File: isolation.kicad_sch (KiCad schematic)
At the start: 39 parts, among them J2 NAPPE_FILAMENT_HT, U1 UCC27517, U12 UCC24612, U13 SN74LVC1G08, U3 ISO7710, U5 DPC817, U7 AMC0311R, U8 AMC0311R, U9 AMC0302R

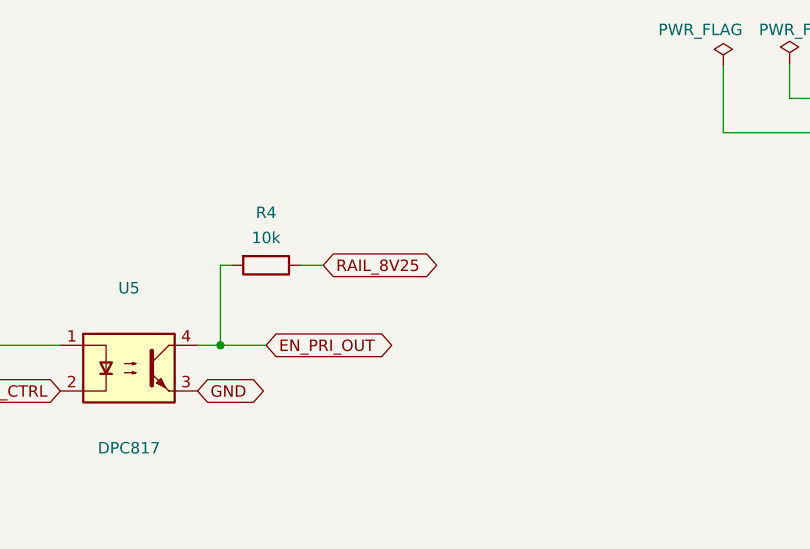
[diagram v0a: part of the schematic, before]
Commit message: Retouches manuelles : notation ~{} pour nPRE/nQ_TRIP, RAIL_8V25->RAIL_3V3_PRI, via 1.0/0.4mm
Renomme nPRE et nQ_TRIP en notation KiCad overline (~{PRE}/~{Q_TRIP}),
corrige une etiquette RAIL_8V25 en RAIL_3V3_PRI dans isolation.kicad_sch,
ajuste la taille de via par defaut (1.8/0.8 -> 1.0/0.4mm) et progresse sur
le placement/routage PCB.

Co-Authored-By: Claude Sonnet 5 <noreply@anthropic.com>
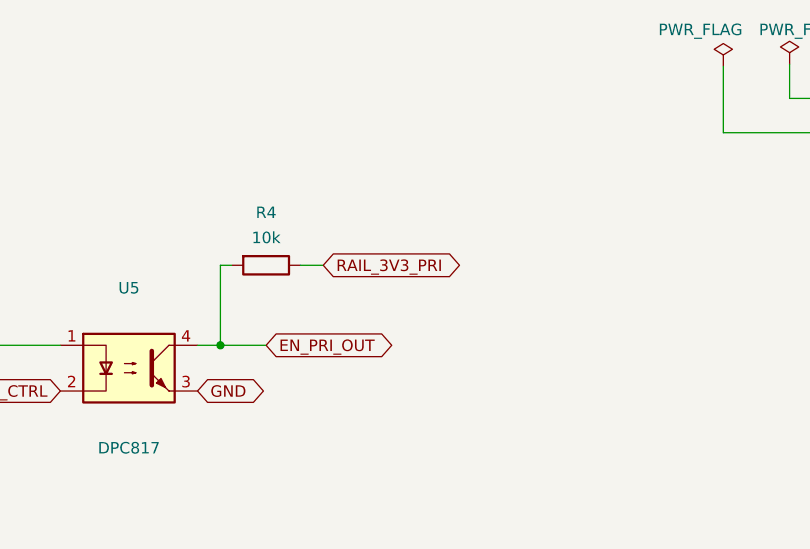
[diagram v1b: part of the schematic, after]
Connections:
- net RAIL_3V3_PRI: now also R4.1
- net RAIL_8V25: no longer R4.1
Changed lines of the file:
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@@
+		)
+	)
+	(global_label "RAIL_3V3_PRI"
+		(shape bidirectional)
+		(at 141.478 50.292 0)
+		(fields_autoplaced yes)
+		(effects
+			(font
+				(size 1.27 1.27)
+			)
+			(justify left)
+		)
+		(property "Intersheetrefs" "${INTERSHEET_REFS}"
+			(at 158.1536 50.292 0)
+			(hide yes)
+			(show_name no)
+			(do_not_autoplace no)
+			(effects
+				(font
+					(size 1.27 1.27)
+				)
+				(justify left)
+			)
 		)
 	)
@@
 			)
 		)
-	)
-	(global_label "RAIL_8V25"
-		(shape bidirectional)
-		(at 141.478 50.292 0)
-		(fields_autoplaced yes)
-		(effects
-			(font
-				(size 1.27 1.27)
-			)
-			(justify left)
-		)
-		(property "Intersheetrefs" "${INTERSHEET_REFS}"
-			(at 155.2507 50.292 0)
-			(hide yes)
-			(show_name no)
-			(do_not_autoplace no)
-			(effects
-				(font
-					(size 1.27 1.27)
-				)
-				(justify left)
-			)
-		)

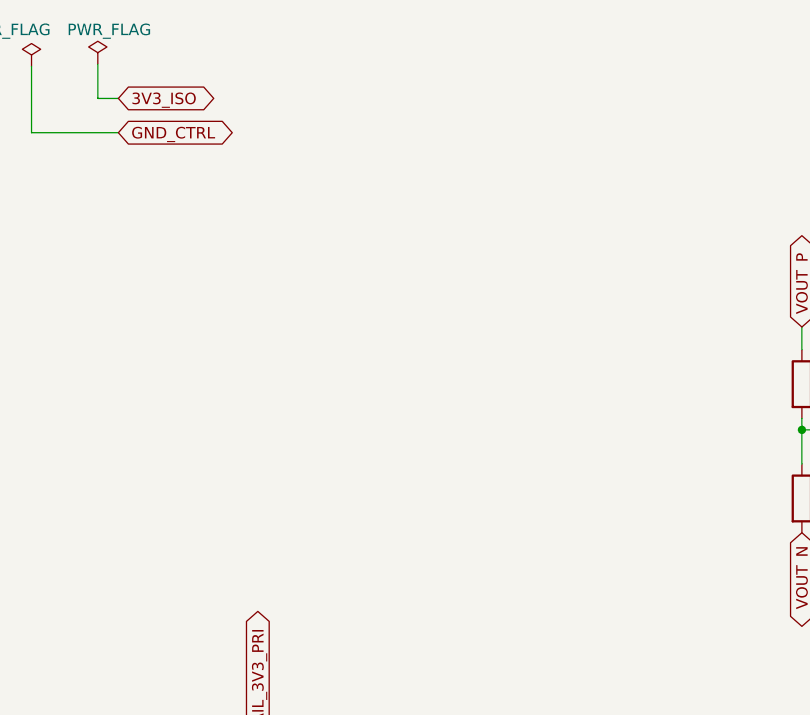
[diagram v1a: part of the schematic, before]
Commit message: Resistances de reference inter-domaines (3x1M par barriere), F1 a 3A
Ajoute les trois chaines de resistances 1M en serie (R35/R6/R36,
R37/R38/R39, R42/R41/R40) qui ferment le point ouvert du plan
d'isolation (S3) : reference DC entre les trois domaines sans degrader
la CMTI. Chaine plutot qu'une resistance unique -- un seul 0805 n'a que
0,8mm d'ecart cuivre entre ses pastilles, loin des 8,5mm vises.

F1 fixe a 3A. TVS directe sur VIN retiree de la liste : deja presente
sur KICAD-C2000-powershield, en amont au niveau systeme.

Nomenclature reverifiee sur tout le projet, aucune collision. Fichiers
touches revalides (equilibre parentheses conscient des chaines,
chargement standalone + hierarchie complete). Documente au S20 de
00-intention-conception.md et dans doc/plan-isolation-4couches.md
(recommandation d'origine << resistance unique sous l'isolateur >>
corrigee).

Co-Authored-By: Claude Sonnet 5 <noreply@anthropic.com>
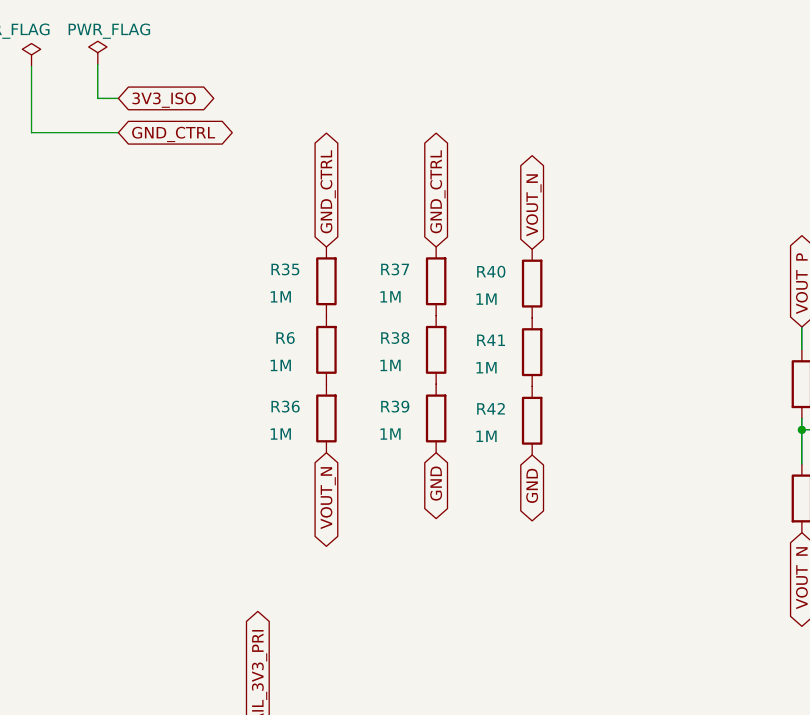
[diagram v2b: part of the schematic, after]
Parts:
- added R35, R36, R37, R38, R39, R40, R41, R42, R6: 1M, Resistor_SMD:R_0805_2012Metric, symbol Device:R
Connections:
- net GND: now also R39.1, R42.1
- net GND_CTRL: now also R35.2, R37.2
- net VOUT_N: now also R36.1, R40.2
- new net: R38.1, R39.2
- new net: R37.1, R38.2
- new net: R40.1, R41.2
- new net: R36.2, R6.1
- new net: R35.1, R6.2
- new net: R41.1, R42.2
